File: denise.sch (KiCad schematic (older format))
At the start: 51 parts, among them CN202 DB23_Female, CN203 Conn_02x18_Odd_Even, CN206 COMPOSITE, CN207 INTERNAL VIDEO SLOT, U201 DENISE8373, U205 74LS244, U206 74LS244, U303 74F08

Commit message: Rename bus with correct syntax
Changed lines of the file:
@@
-EESchema Schematic File Version 4
+EESchema Schematic File Version 5
 LIBS:amiga2000-cache
 EELAYER 29 0
@@
 	1700 5200 1800 5300
 Text GLabel 1500 2550 0    50   Input ~ 0
-DRD(0:15)
+DRD[0..15]
 Text GLabel 1500 4400 0    50   Input ~ 0
-RGA(1:8)
+RGA[1..8]
 Wire Bus Line
 	1500 2550 1700 2550
@@
 	3850 900  3950 1000
 Text GLabel 3450 900  0    50   Input ~ 0
-R(0:3)
+R[0..3]
 Wire Wire Line
 	4050 800  3100 800
@@
 	3000 1000 2900 1000
 Text GLabel 2900 1000 0    50   Input ~ 0
-G(0:3)
+G[0..3]
 Wire Wire Line
 	4250 1150 4250 700
@@
 	2600 700  2700 600
 Text GLabel 2750 600  2    50   Input ~ 0
-B(0:3)
+B[0..3]
 Wire Wire Line
 	4550 1150 4550 900
@@
 Connection ~ 6150 800
 Text GLabel 6250 800  2    50   Input ~ 0
-PPD(0:7)
+PPD[0..7]
 Text GLabel 7550 2100 0    50   Input ~ 0
 FLTLEFT
@@
 	11300 2650 11350 2650
 Text GLabel 11350 2650 2    50   Input ~ 0
-R(0:3)
+R[0..3]
 Text GLabel 11350 3100 2    50   Input ~ 0
-B(0:3)
+B[0..3]
 Text GLabel 11350 2850 2    50   Input ~ 0
-G(0:3)
+G[0..3]
 $Comp
 L Device:C_Feedthrough EMI208
@@
 	7400 3750 7500 3650
 Text GLabel 7450 3550 0    50   Input ~ 0
-R(0:3)
+R[0..3]
 Text GLabel 6900 5900 0    50   Input ~ 0
-B(0:3)
+B[0..3]
 Text GLabel 7600 5900 0    50   Input ~ 0
-G(0:3)
+G[0..3]
 Wire Bus Line
 	7550 3650 7550 3550
@@
 Wire Wire Line
 	9100 3850 9100 5250
+Connection ~ 5900 4000
+Wire Wire Line
+	5900 4000 5650 4000
 Wire Bus Line
 	11300 2950 11300 3100
@@
 Wire Bus Line
 	1700 2550 1700 4150
-Connection ~ 5900 4000
-Wire Wire Line
-	5900 4000 5650 4000
 $EndSCHEMATC

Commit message: squeak
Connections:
- net GND: now also C206.1, U205.19 (OEb), U206.1 (OEa); no longer C206.2
- net at C205.1, C214.1, C226.1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: now also C206.2; no longer C206.1
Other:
- moved on the sheet: C206
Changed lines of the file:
@@
 L power:GND #PWR0227
 U 1 1 6E990171
-P 10550 1850
-F 0 "#PWR0227" H 10550 1600 50  0001 C CNN
-F 1 "GND" H 10555 1677 50  0000 C CNN
-F 2 "" H 10550 1850 50  0001 C CNN
-F 3 "" H 10550 1850 50  0001 C CNN
-	1    10550 1850
-	-1   0    0    -1
+P 10300 1900
+F 0 "#PWR0227" H 10300 1650 50  0001 C CNN
+F 1 "GND" H 10305 1727 50  0000 C CNN
+F 2 "" H 10300 1900 50  0001 C CNN
+F 3 "" H 10300 1900 50  0001 C CNN
+	1    10300 1900
+	0    1    -1   0
 $EndComp
 Wire Wire Line
@@
 	3050 6650 3050 6800
 Connection ~ 3050 6650
-Wire Wire Line
-	3050 6650 2800 6650
 $Comp
 L power:+5V #PWR0208
@@
 Wire Wire Line
 	2100 6100 2100 6450
-Wire Wire Line
-	1850 6450 1950 6450
 Connection ~ 2100 6450
 Wire Wire Line
 	2100 6450 2100 6650
 Wire Wire Line
-	2800 6850 2800 6650
-Connection ~ 2800 6650
-Wire Wire Line
-	2800 6650 2650 6650
-Wire Wire Line
 	1650 6850 1650 6650
 Wire Wire Line
 	2100 6650 2350 6650
 Wire Wire Line
-	1650 6850 2800 6850
-Wire Wire Line
-	1950 6450 1950 7250
-Wire Wire Line
-	1950 7250 3700 7250
-Wire Wire Line
 	3700 7250 3700 7000
-Connection ~ 1950 6450
-Wire Wire Line
-	1950 6450 2100 6450
 Wire Wire Line
 	3700 7250 3850 7250
 Wire Wire Line
 	3850 7250 3850 7000
-Connection ~ 3700 7250
 Wire Wire Line
 	4500 7250 4500 7000
@@
 Wire Wire Line
 	6150 4350 6400 4350
-Wire Wire Line
-	5650 4000 5650 3950
-Wire Wire Line
-	5650 4000 5650 4250
-Connection ~ 5650 4000
 $Comp
 L Device:C C205
@@
 L Device:C C206
 U 1 1 7001040C
-P 5200 4350
-F 0 "C206" V 4948 4350 50  0000 C CNN
-F 1 "0.1uF" V 5039 4350 50  0000 C CNN
-F 2 "" H 5238 4200 50  0001 C CNN
-F 3 "~" H 5200 4350 50  0001 C CNN
-	1    5200 4350
-	0    1    1    0
+P 5200 4250
+F 0 "C206" V 4948 4250 50  0000 C CNN
+F 1 "0.1uF" V 5039 4250 50  0000 C CNN
+F 2 "" H 5238 4100 50  0001 C CNN
+F 3 "~" H 5200 4250 50  0001 C CNN
+	1    5200 4250
+	0    -1   -1   0
 $EndComp
 $Comp
@@
 	5000 3900 5000 3950
 Wire Wire Line
-	5000 4350 5050 4350
+	5000 4250 5050 4250
 Wire Wire Line
 	5050 3950 5000 3950
 Connection ~ 5000 3950
 Wire Wire Line
-	5000 3950 5000 4350
+	5000 3950 5000 4250
 Wire Wire Line
 	5350 3950 5650 3950
@@
 Wire Wire Line
 	5650 4250 5350 4250
-Wire Wire Line
-	5350 4250 5350 4350
 Connection ~ 5650 4250
 Wire Wire Line
@@
 Connection ~ 5650 5900
 Wire Wire Line
-	6150 4000 5900 4000
-Wire Wire Line
-	9100 3850 5900 3850
-Wire Wire Line
-	5900 3850 5900 4000
+	9100 3850 6150 3850
 Wire Wire Line
 	9100 3850 9100 5250
-Connection ~ 5900 4000
-Wire Wire Line
-	5900 4000 5650 4000
+Wire Wire Line
+	5150 5600 5150 5500
+Connection ~ 5150 5600
+Connection ~ 5150 5500
+Wire Wire Line
+	5650 3950 5650 4250
+Wire Wire Line
+	5650 3950 6150 3950
+Wire Wire Line
+	6150 3950 6150 4000
+Wire Wire Line
+	6150 3850 6150 3950
+Connection ~ 6150 3950
+Wire Wire Line
+	1850 6450 2100 6450
+Wire Wire Line
+	3700 7250 2100 7250
+Wire Wire Line
+	2100 7250 2100 6650
+Connection ~ 3700 7250
+Connection ~ 2100 6650
+Wire Wire Line
+	2650 6650 3050 6650
+$Comp
+L power:GND #PWR0261
+U 1 1 5DA315FD
+P 1650 6850
+F 0 "#PWR0261" H 1650 6600 50  0001 C CNN
+F 1 "GND" H 1655 6677 50  0000 C CNN
+F 2 "" H 1650 6850 50  0001 C CNN
+F 3 "" H 1650 6850 50  0001 C CNN
+	1    1650 6850
+	-1   0    0    -1
+$EndComp
+Wire Wire Line
+	10300 1900 10550 1900
+Wire Wire Line
+	10550 1900 10550 1850
 Wire Bus Line
 	11300 2950 11300 3100

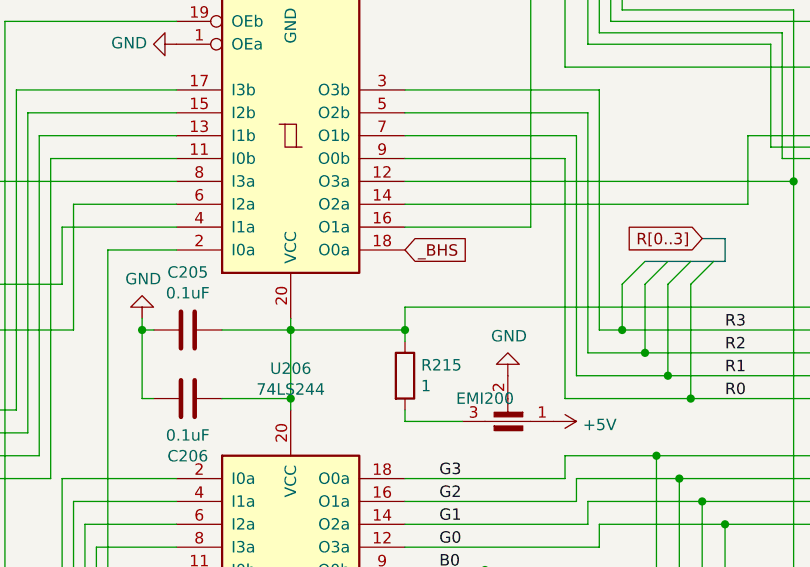
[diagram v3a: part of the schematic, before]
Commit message: More final ERC fixes
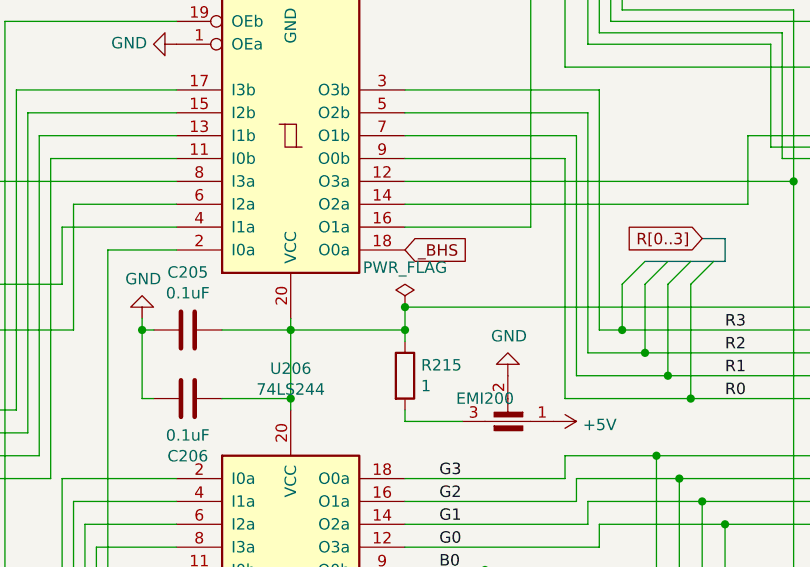
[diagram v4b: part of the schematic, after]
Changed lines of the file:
@@
 Wire Bus Line
 	1700 2550 1700 4150
+$Comp
+L power:PWR_FLAG #FLG?
+U 1 1 5DAEFE05
+P 6150 3850
+F 0 "#FLG?" H 6150 3925 50  0001 C CNN
+F 1 "PWR_FLAG" H 6150 4023 50  0000 C CNN
+F 2 "" H 6150 3850 50  0001 C CNN
+F 3 "~" H 6150 3850 50  0001 C CNN
+	1    6150 3850
+	1    0    0    -1
+$EndComp
+Connection ~ 6150 3850
 $EndSCHEMATC
